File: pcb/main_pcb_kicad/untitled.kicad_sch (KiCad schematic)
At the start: 0 parts

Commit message: Added everything to main schematic
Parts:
- added C1, C8: 1u, Capacitor_SMD:C_0402_1005Metric, symbol Device:C
- added C10, C2, C3, C4, C5, C6, C7, C9: 100n, Capacitor_SMD:C_0402_1005Metric, symbol Device:C
- added C11, C12: 10u, Capacitor_SMD:C_0402_1005Metric, symbol Device:C
- added C13, C14: 15p, Capacitor_SMD:C_0402_1005Metric, symbol Device:C
- added J1: USB_B_Micro, Connector_USB:USB_Micro-B_Amphenol_10118194_Horizontal, symbol Connector:USB_B_Micro
- added J2: Conn_01x03, Connector_PinHeader_2.54mm:PinHeader_1x03_P2.54mm_Vertical, symbol Connector_Generic:Conn_01x03
- added R1: 10k, Resistor_SMD:R_0402_1005Metric, symbol Device:R
- added R2, R5: 1k, Resistor_SMD:R_0402_1005Metric, symbol Device:R
- added R3, R4: 27, Resistor_SMD:R_0402_1005Metric, symbol Device:R
- added SW1: SW_Push, SKRPABE010, symbol Switch:SW_SPST
- added SW2: SW_Push, SKRPABE010, symbol Switch:SW_Push
- added U1: RP2040, Package_DFN_QFN:QFN-56-1EP_7x7mm_P0.4mm_EP3.2x3.2mm, symbol MCU_RaspberryPi:RP2040
- added U2: W25Q16JVUXIQ TR, USON-8-EP (2 x 3 mm), symbol Memory_Flash:W25Q128JVS
- added U3: NCP1117-3.3_SOT223, Package_TO_SOT_SMD:SOT-223-3_TabPin2, symbol Regulator_Linear:NCP1117-3.3_SOT223
- added Y1: ABM8-272-T3, 3.2x2.5mm, symbol Device:Crystal_GND24
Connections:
- new net: R3.2, U1.46 (USB_DM)
- new net: J2.1 (Pin_1), U1.24 (SWCLK)
- new net: J2.3 (Pin_3), U1.25 (SWDIO)
- new net: SW2.2, U1.26 (RUN)
- new net: R4.2, U1.47 (USB_DP)
- new net: C14.2, R5.1, Y1.3
- new net: C11.1, J1.1 (VBUS), U3.3 (VI)
- new net +1V1: C1.1, C2.1, C9.1, U1.23 (DVDD), U1.45 (VREG_VOUT), U1.50 (DVDD)
- new net +3V3: C10.1, C12.1, C3.1, C4.1, C5.1, C6.1, C7.1, C8.1, R1.1, U1.1 (IOVDD), U1.10 (IOVDD), U1.22 (IOVDD), U1.33 (IOVDD), U1.42 (IOVDD), U1.43 (ADC_AVDD), U1.44 (VREG_VIN), U1.48 (USB_VDD), U1.49 (IOVDD), U2.8 (VCC), U3.2 (VO)
- new net GND: C1.2, C10.2, C11.2, C12.2, C13.1, C14.1, C2.2, C3.2, C4.2, C5.2, C6.2, C7.2, C8.2, C9.2, J1.5 (GND), J1.SH (Shield), J2.2 (Pin_2), SW1.1 (A), SW2.1, U1.19 (TESTEN), U1.57 (GND), U2.4 (GND), U3.1 (GND), Y1.2 (G), Y1.4 (G)
- new net QSPI_CLK: U1.52 (QSPI_SCLK), U2.6 (CLK)
- new net QSPI_CS: R1.2, R2.2, U1.56 (~{QSPI_SS}), U2.1 (~{CS})
- new net QSPI_SD0: U1.53 (QSPI_SD0), U2.5 (DI/IO_{0})
- new net QSPI_SD1: U1.55 (QSPI_SD1), U2.2 (DO/IO_{1})
- new net QSPI_SD2: U1.54 (QSPI_SD2), U2.3 (~{WP}/IO_{2})
- new net QSPI_SD3: U1.51 (QSPI_SD3), U2.7 (~{HOLD}/~{RESET}/IO_{3})
- new net SCL: U1.2 (GPIO0)
- new net SDA: U1.3 (GPIO1)
- new net USB_D+: J1.3 (D+), R4.1
- new net USB_D-: J1.2 (D-), R3.1
- new net XIN: C13.2, U1.20 (XIN), Y1.1
- new net XOUT: R5.2, U1.21 (XOUT)
- new net ~{USB_BOOT}: R2.1, SW1.2 (B)
- no-connect marks 0 -> 29
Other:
- note added: "Crystal"
- note added: "Decoupling Capacitors"
- note added: "Flash Storage"
- note added: "Place 1u caps close to VREG_VIN and VREG_VOUT"
- note added: "Power"

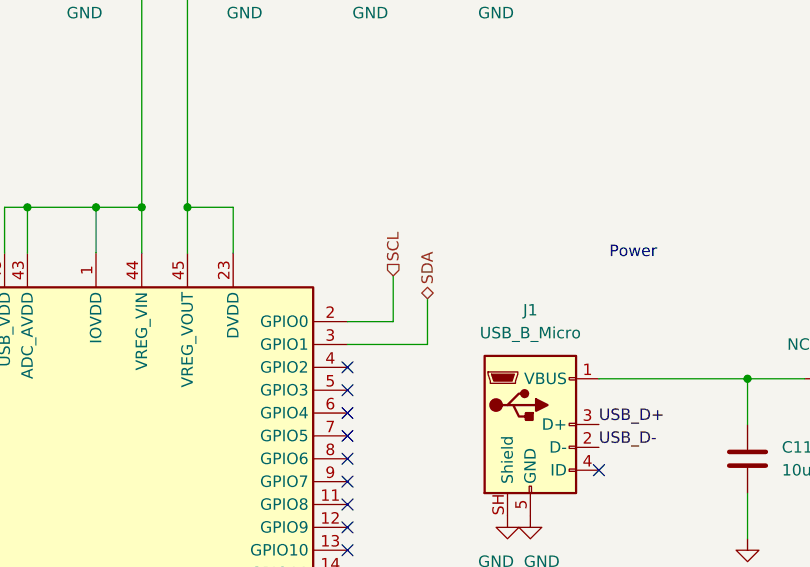
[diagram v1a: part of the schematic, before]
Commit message: i fixed the layout on the MCU for SDA and SCL also added page information on the subsheets
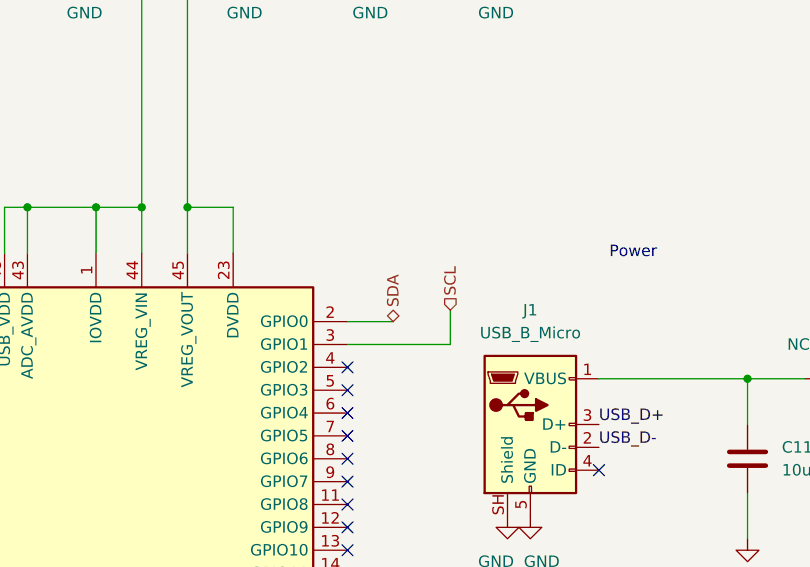
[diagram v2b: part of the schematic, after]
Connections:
- net SCL: now also U1.3 (GPIO1); no longer U1.2 (GPIO0)
- net SDA: now also U1.2 (GPIO0); no longer U1.3 (GPIO1)
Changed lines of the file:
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@@
 	(wire
 		(pts
-			(xy 165.1 87.63) (xy 173.99 87.63)
+			(xy 165.1 87.63) (xy 176.53 87.63)
 		)
 		(stroke
@@
 	(wire
 		(pts
-			(xy 173.99 82.55) (xy 173.99 87.63)
-		)
-		(stroke
-			(width 0)
-			(type default)
-		)
-	)
-	(wire
-		(pts
 			(xy 121.92 41.91) (xy 121.92 45.72)
 		)
@@
 	(wire
 		(pts
+			(xy 176.53 87.63) (xy 176.53 83.82)
+		)
+		(stroke
+			(width 0)
+			(type default)
+		)
+	)
+	(wire
+		(pts
 			(xy 72.39 86.36) (xy 72.39 90.17)
 		)
@@
 		(pts
 			(xy 152.4 72.39) (xy 147.32 72.39)
-		)
-		(stroke
-			(width 0)
-			(type default)
-		)
-	)
-	(wire
-		(pts
-			(xy 170.18 80.01) (xy 170.18 85.09)
 		)
 		(stroke
@@
 	(hierarchical_label "SCL"
 		(shape input)
-		(at 170.18 80.01 90)
+		(at 176.53 83.82 90)
 		(effects
 			(font
@@
 	(hierarchical_label "SDA"
 		(shape bidirectional)
-		(at 173.99 82.55 90)
-		(effects
-			(font
+		(at 170.18 85.09 90)
+		(effects
+			(font

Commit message: added some comments
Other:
- note added: "THE SDA AND SCL PULL UPS ARE ON THE COLOR SENSOR SHEET"
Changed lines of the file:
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@@
 	(text "Power\n"
 		(exclude_from_sim no)
-		(at 196.85 77.47 0)
+		(at 199.39 83.82 0)
 		(effects
 			(font
@@
 			)
 		)
+	)
+	(text "THE SDA AND SCL PULL UPS\nARE ON THE COLOR SENSOR SHEET"
+		(exclude_from_sim no)
+		(at 182.88 72.39 0)
+		(effects
+			(font
+				(size 1.905 1.905)
+			)
+		)

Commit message: work was done
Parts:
- removed U3: NCP1117-3.3_SOT223, Package_TO_SOT_SMD:SOT-223-3_TabPin2, symbol Regulator_Linear:NCP1117-3.3_SOT223
- added U10: AP2112K-3.3, Package_TO_SOT_SMD:SOT-23-5, symbol Regulator_Linear:AP2112K-3.3
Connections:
- net +3V3: now also U10.5 (VOUT)
- net GND: now also U10.2 (GND)
- net at C11.1, J1.1 (VBUS): now also U10.1 (VIN)
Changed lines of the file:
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@@
 	)
 	(junction
-		(at 245.11 91.44)
+		(at 63.5 90.17)
 		(diameter 0)
 		(color 0 0 0 0)
 	)
 	(junction
-		(at 63.5 90.17)
+		(at 58.42 173.99)
 		(diameter 0)
 		(color 0 0 0 0)
 	)
 	(junction
-		(at 58.42 173.99)
+		(at 209.55 91.44)
 		(diameter 0)
 		(color 0 0 0 0)
@@
 	)
 	(junction
-		(at 209.55 91.44)
-		(diameter 0)
-		(color 0 0 0 0)
-	)
-	(junction
 		(at 72.39 90.17)
 		(diameter 0)
@@
 	)
 	(junction
+		(at 245.11 88.9)
+		(diameter 0)
+		(color 0 0 0 0)
+	)
+	(junction
 		(at 121.92 30.48)
 		(diameter 0)
@@
 	(wire
 		(pts
-			(xy 231.14 91.44) (xy 245.11 91.44)
-		)
-		(stroke
-			(width 0)
-			(type default)
-		)
-	)
-	(wire
-		(pts
 			(xy 58.42 160.02) (xy 58.42 165.1)
 		)
@@
 	(wire
 		(pts
+			(xy 209.55 88.9) (xy 215.9 88.9)
+		)
+		(stroke
+			(width 0)
+			(type default)
+		)
+	)
+	(wire
+		(pts
 			(xy 27.94 168.91) (xy 27.94 160.02)
 		)
@@
 	(wire
 		(pts
+			(xy 209.55 91.44) (xy 209.55 88.9)
+		)
+		(stroke
+			(width 0)
+			(type default)
+		)
+	)
+	(wire
+		(pts
 			(xy 181.61 25.4) (xy 181.61 30.48)
 		)
@@
 	(wire
 		(pts
-			(xy 58.42 173.99) (xy 63.5 173.99)
+			(xy 209.55 91.44) (xy 209.55 96.52)
 		)
 		(stroke
@@
 	(wire
 		(pts
-			(xy 109.22 30.48) (xy 121.92 30.48)
+			(xy 58.42 173.99) (xy 63.5 173.99)
 		)
 		(stroke
@@
 	(wire
 		(pts
-			(xy 193.04 91.44) (xy 209.55 91.44)
+			(xy 109.22 30.48) (xy 121.92 30.48)
 		)
 		(stroke
@@
 	(wire
 		(pts
-			(xy 58.42 172.72) (xy 58.42 173.99)
+			(xy 193.04 91.44) (xy 209.55 91.44)
 		)
 		(stroke
@@
 	(wire
 		(pts
-			(xy 245.11 86.36) (xy 245.11 91.44)
+			(xy 58.42 172.72) (xy 58.42 173.99)
 		)
 		(stroke
@@
 	(wire
 		(pts
-			(xy 101.6 158.75) (xy 105.41 158.75)
+			(xy 245.11 86.36) (xy 245.11 88.9)
 		)
 		(stroke
@@
 	(wire
 		(pts
-			(xy 49.53 62.23) (xy 39.37 62.23)
+			(xy 231.14 88.9) (xy 245.11 88.9)
 		)
 		(stroke
@@
 	(wire
 		(pts
-			(xy 106.68 100.33) (xy 106.68 96.52)
+			(xy 101.6 158.75) (xy 105.41 158.75)
 		)
 		(stroke
@@
 	(wire
 		(pts
-			(xy 245.11 101.6) (xy 245.11 104.14)
+			(xy 49.53 62.23) (xy 39.37 62.23)
 		)
 		(stroke
@@
 	(wire
 		(pts
-			(xy 245.11 91.44) (xy 245.11 93.98)
+			(xy 106.68 100.33) (xy 106.68 96.52)
 		)
 		(stroke
@@
 	(wire
 		(pts
-			(xy 44.45 123.19) (xy 49.53 123.19)
+			(xy 245.11 101.6) (xy 245.11 104.14)
 		)
 		(stroke
@@
 	(wire
 		(pts
-			(xy 31.75 127) (xy 31.75 123.19)
+			(xy 245.11 88.9) (xy 245.11 93.98)
 		)
 		(stroke
@@
 	(wire
 		(pts
-			(xy 209.55 91.44) (xy 209.55 96.52)
+			(xy 44.45 123.19) (xy 49.53 123.19)
 		)
 		(stroke
@@
 	(wire
 		(pts
-			(xy 209.55 91.44) (xy 215.9 91.44)
+			(xy 31.75 127) (xy 31.75 123.19)
 		)
 		(stroke
@@
 	)
 	(symbol
+		(lib_id "Regulator_Linear:AP2112K-3.3")
+		(at 223.52 91.44 0)
+		(unit 1)
+		(body_style 1)
+		(exclude_from_sim no)
+		(in_bom yes)
+		(on_board yes)
+		(in_pos_files yes)
+		(dnp no)
+		(fields_autoplaced yes)
+		(property "Reference" "U10"
+			(at 223.52 82.55 0)
+			(show_name no)
+			(do_not_autoplace no)
+			(effects
+				(font
+					(size 1.27 1.27)
+				)
+			)
+		)
+		(property "Value" "AP2112K-3.3"
+			(at 223.52 85.09 0)
+			(show_name no)
+			(do_not_autoplace no)
+			(effects
+				(font
+					(size 1.27 1.27)
+				)
+			)
+		)
+		(property "Footprint" "Package_TO_SOT_SMD:SOT-23-5"
+			(at 223.52 83.185 0)
+			(hide yes)
+			(show_name no)
+			(do_not_autoplace no)
+			(effects
+				(font
+					(size 1.27 1.27)
+				)
+			)
+		)
+		(property "Datasheet" "https://www.diodes.com/assets/Datasheets/AP2112.pdf"
+			(at 223.52 88.9 0)
+			(hide yes)
+			(show_name no)
+			(do_not_autoplace no)
+			(effects
+				(font
+					(size 1.27 1.27)
+				)
+			)
+		)
+		(property "Description" "600mA low dropout linear regulator, with enable pin, 3.8V-6V input voltage range, 3.3V fixed positive output, SOT-23-5"
+			(at 223.52 91.44 0)
+			(hide yes)
+			(show_name no)
+			(do_not_autoplace no)
+			(effects
+				(font
+					(size 1.27 1.27)
+				)
+			)
+		)
+		(pin "5"
+		)
+		(pin "1"
+		)
+		(pin "3"
+		)
+		(pin "2"
+		)
+		(pin "4"
+		)
+		(instances
+			(project "main_pcb_project"
+				(path "/9164435f-a95c-403a-a8b4-52de8af1bdc8/43d08942-0182-4d4a-9589-a975afa41050"
+					(reference "U10")
+					(unit 1)
+				)
+			)
+		)
+	)
+	(symbol
 		(lib_id "power:+3V3")
 		(at 245.11 86.36 0)
@@
 					(unit 1)
 				)
-			)
-		)
-	)
-	(symbol
-		(lib_id "Regulator_Linear:NCP1117-3.3_SOT223")
-		(at 223.52 91.44 0)
-		(unit 1)
-		(body_style 1)
-		(exclude_from_sim no)
-		(in_bom yes)
-		(on_board yes)
-		(in_pos_files yes)
-		(dnp no)
-		(fields_autoplaced yes)
-		(property "Reference" "U3"
-			(at 223.52 85.09 0)
-			(show_name no)
-			(do_not_autoplace no)
-			(effects
-				(font
-					(size 1.27 1.27)
-				)
-			)
-		)
-		(property "Value" "NCP1117-3.3_SOT223"
-			(at 223.52 87.63 0)
-			(show_name no)
-			(do_not_autoplace no)
-			(effects
-				(font
-					(size 1.27 1.27)
-				)
-			)
-		)
-		(property "Footprint" "Package_TO_SOT_SMD:SOT-223-3_TabPin2"
-			(at 223.52 86.36 0)
-			(hide yes)
-			(show_name no)
-			(do_not_autoplace no)
-			(effects
-				(font
-					(size 1.27 1.27)
-				)
-			)
-		)
-		(property "Datasheet" "http://www.onsemi.com/pub_link/Collateral/NCP1117-D.PDF"
-			(at 226.06 97.79 0)
-			(hide yes)
-			(show_name no)
-			(do_not_autoplace no)
-			(effects
-				(font
-					(size 1.27 1.27)
-				)
-			)
-		)
-		(property "Description" "1A Low drop-out regulator, Fixed Output 3.3V, SOT-223"
-			(at 223.52 91.44 0)
-			(hide yes)
-			(show_name no)
-			(do_not_autoplace no)
-			(effects
-				(font
-					(size 1.27 1.27)
-				)
-			)
-		)
-		(property "Manufacturer P/N" ""
-			(at 223.52 91.44 0)
-			(hide yes)
-			(show_name no)
-			(do_not_autoplace no)
-			(effects
-				(font
-					(size 1.27 1.27)
-				)
-			)
-		)
-		(property "Vendor" ""
-			(at 223.52 91.44 0)
-			(hide yes)
-			(show_name no)
-			(do_not_autoplace no)
-			(effects
-				(font
-					(size 1.27 1.27)
-				)
-			)
-		)
-		(property "Vendor P/N" ""
-			(at 223.52 91.44 0)
-			(hide yes)
-			(show_name no)
-			(do_not_autoplace no)
-			(effects
-				(font
-					(size 1.27 1.27)
-				)
-			)
-		)
-		(pin "1"
-		)
-		(pin "2"
-		)
-		(pin "3"
-		)
-		(instances
-			(project "main_pcb_project"
-				(path "/9164435f-a95c-403a-a8b4-52de8af1bdc8/43d08942-0182-4d4a-9589-a975afa41050"
-					(reference "U3")
-					(unit 1)
-				)

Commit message: worked on the SPI
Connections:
- net at C11.1, J1.1 (VBUS), U10.1 (VIN): now also U10.3 (EN)
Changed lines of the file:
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@@
+	(wire
+		(pts
+			(xy 209.55 91.44) (xy 215.9 91.44)
+		)
+		(stroke
+			(width 0)
+			(type default)
+		)
+	)
 	(wire
 		(pts

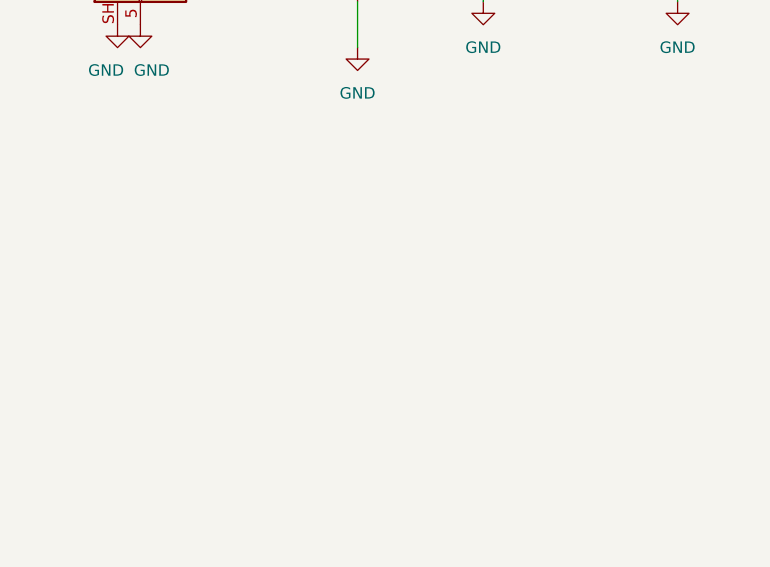
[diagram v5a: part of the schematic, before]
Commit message: Adding footprints
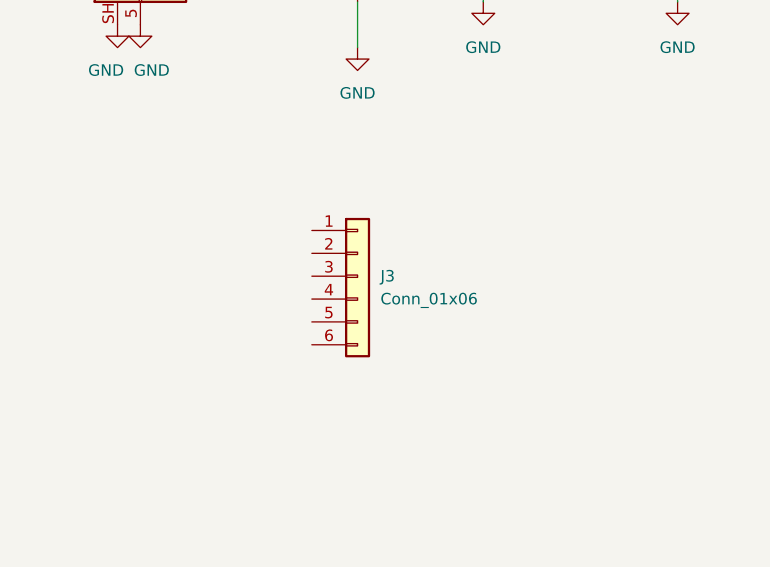
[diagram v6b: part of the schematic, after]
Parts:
- added J3: Conn_01x06, Connector_JST:JST_PH_S6B-PH-K_1x06_P2.00mm_Horizontal, symbol Connector_Generic:Conn_01x06
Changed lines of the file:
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@@
+	)
+	(symbol
+		(lib_id "Connector_Generic:Conn_01x06")
+		(at 209.55 134.62 0)
+		(unit 1)
+		(body_style 1)
+		(exclude_from_sim no)
+		(in_bom yes)
+		(on_board yes)
+		(in_pos_files yes)
+		(dnp no)
+		(fields_autoplaced yes)
+		(property "Reference" "J3"
+			(at 212.09 134.6199 0)
+			(show_name no)
+			(do_not_autoplace no)
+			(effects
+				(font
+					(size 1.27 1.27)
+				)
+				(justify left)
+			)
+		)
+		(property "Value" "Conn_01x06"
+			(at 212.09 137.1599 0)
+			(show_name no)
+			(do_not_autoplace no)
+			(effects
+				(font
+					(size 1.27 1.27)
+				)
+				(justify left)
+			)
+		)
+		(property "Footprint" "Connector_JST:JST_PH_S6B-PH-K_1x06_P2.00mm_Horizontal"
+			(at 209.55 134.62 0)
+			(hide yes)
+			(show_name no)
+			(do_not_autoplace no)
+			(effects
+				(font
+					(size 1.27 1.27)
+				)
+			)
+		)
+		(property "Datasheet" ""
+			(at 209.55 134.62 0)
+			(hide yes)
+			(show_name no)
+			(do_not_autoplace no)
+			(effects
+				(font
+					(size 1.27 1.27)
+				)
+			)
+		)
+		(property "Description" "Generic connector, single row, 01x06, script generated (kicad-library-utils/schlib/autogen/connector/)"
+			(at 209.55 134.62 0)
+			(hide yes)
+			(show_name no)
+			(do_not_autoplace no)
+			(effects
+				(font
+					(size 1.27 1.27)
+				)
+			)
+		)
+		(property "Manufacturer P/N" ""
+			(at 209.55 134.62 0)
+			(hide yes)
+			(show_name no)
+			(do_not_autoplace no)
+			(effects
+				(font
+					(size 1.27 1.27)
+				)
+			)
+		)
+		(property "Vendor" ""
+			(at 209.55 134.62 0)
+			(hide yes)
+			(show_name no)
+			(do_not_autoplace no)
+			(effects
+				(font
+					(size 1.27 1.27)
+				)
+			)
+		)
+		(property "Vendor P/N" ""
+			(at 209.55 134.62 0)
+			(hide yes)
+			(show_name no)
+			(do_not_autoplace no)
+			(effects
+				(font
+					(size 1.27 1.27)
+				)
+			)
+		)
+		(pin "6"
+		)
+		(pin "5"
+		)
+		(pin "1"
+		)
+		(pin "3"
+		)
+		(pin "2"
+		)
+		(pin "4"
+		)
+		(instances
+			(project "main_pcb_project"
+				(path "/9164435f-a95c-403a-a8b4-52de8af1bdc8/43d08942-0182-4d4a-9589-a975afa41050"
+					(reference "J3")
+					(unit 1)
+				)
+			)
+		)
 	)
 	(symbol

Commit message: Adding more footprints
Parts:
- SW1, SW2: footprint SKRPABE010 -> footprints:SW_SKRPACE010_AAL
- U2: footprint USON-8-EP (2 x 3 mm) -> footprints:USON-8_UX_2x3x0p6_WIN
- Y1: footprint 3.2x2.5mm -> footprints:ABM8-272-T3_ABR
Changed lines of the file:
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@@
 			)
 		)
-		(property "Footprint" "SKRPABE010"
+		(property "Footprint" "footprints:SW_SKRPACE010_AAL"
 			(at 88.9 91.44 0)
 			(hide yes)
@@
 			)
 		)
-		(property "Footprint" "SKRPABE010"
+		(property "Footprint" "footprints:SW_SKRPACE010_AAL"
 			(at 39.37 123.19 0)
 			(hide yes)
@@
 			)
 		)
-		(property "Footprint" "3.2x2.5mm"
+		(property "Footprint" "footprints:ABM8-272-T3_ABR"
 			(at 58.42 168.91 0)
 			(hide yes)
@@
 			)
 		)
-		(property "Footprint" "USON-8-EP (2 x 3 mm)"
+		(property "Footprint" "footprints:USON-8_UX_2x3x0p6_WIN"
 			(at 49.53 74.93 0)
 			(hide yes)
